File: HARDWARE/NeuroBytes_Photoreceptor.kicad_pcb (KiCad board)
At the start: 2 copper layers, 46.8 x 19.8 mm, 24 parts, among them P1 JST_GH_4-POS, P2 JST_GH_4-POS, P3 JST_GH_5-pos, SW1 SW_PB_4term, SW2 SW_PB_4term, U1 APDS9007, U2 STM32L011Gx, U3 3v3 LDO

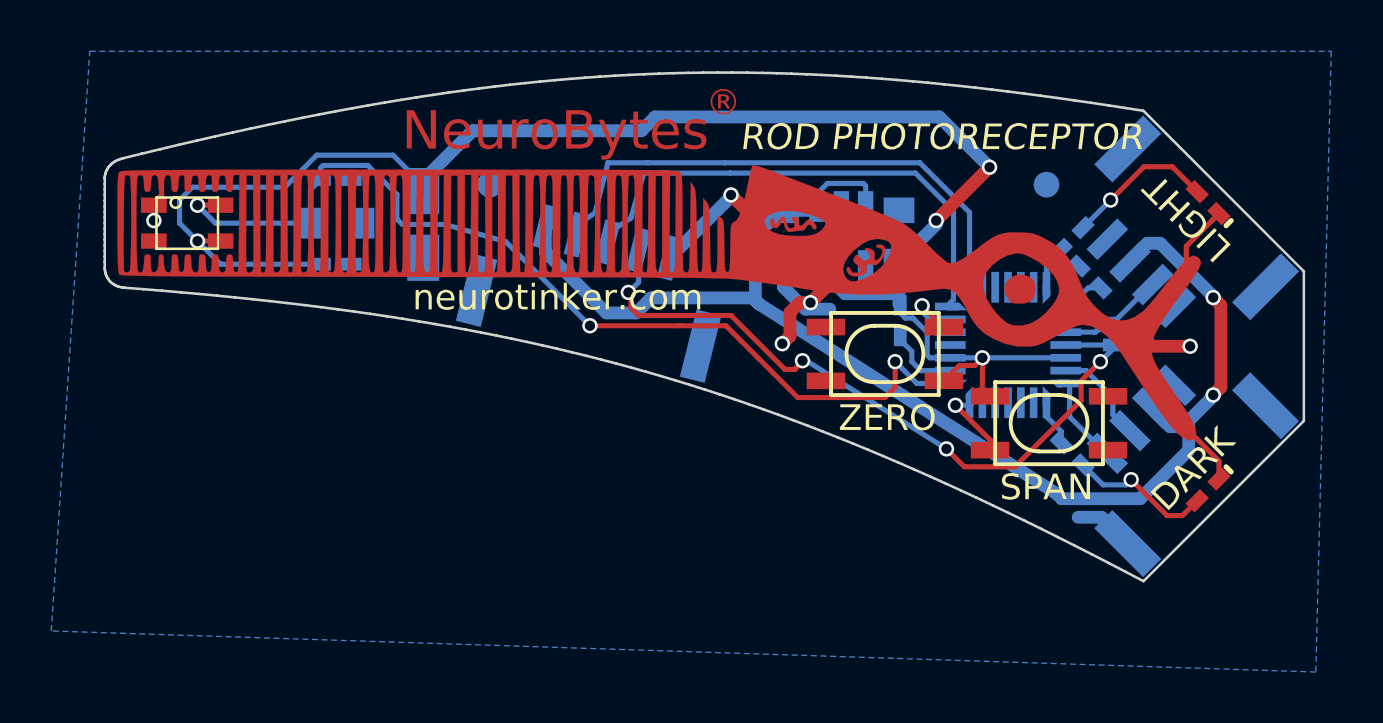
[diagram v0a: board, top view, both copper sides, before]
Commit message: added ESD protection. updated title block. minor routing changes.
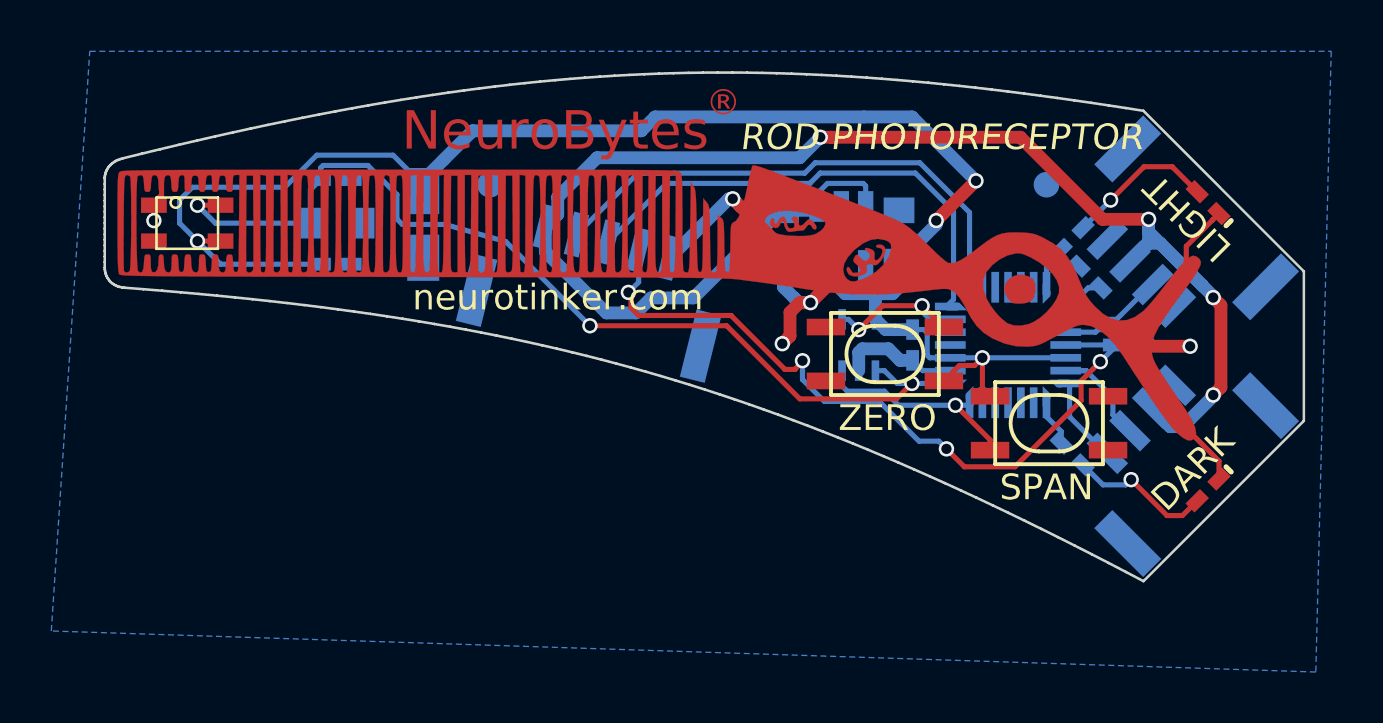
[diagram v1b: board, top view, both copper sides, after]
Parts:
- added U4: RClamp0503F, KiCad_Footprints:ZF_SMD_SOT-353, B.Cu at (194.2, 100.8)
- moved C6 1.06 mm to (196.3, 100.8)
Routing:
- net +5V: track 52.3 -> 61.7 mm, vias 2 -> 4
- net SPAN: track 3.15 -> 8.48 mm
- net ZERO: track 2.77 -> 6.44 mm, vias 1 -> 2
- net RESET: track 28.1 -> 29.7 mm
- net GND: track 54.8 -> 53.3 mm
- net SENSE: track 38.6 -> 39.3 mm
- net +3V3: track 66.0 -> 65.4 mm
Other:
- board text removed: "POWER"

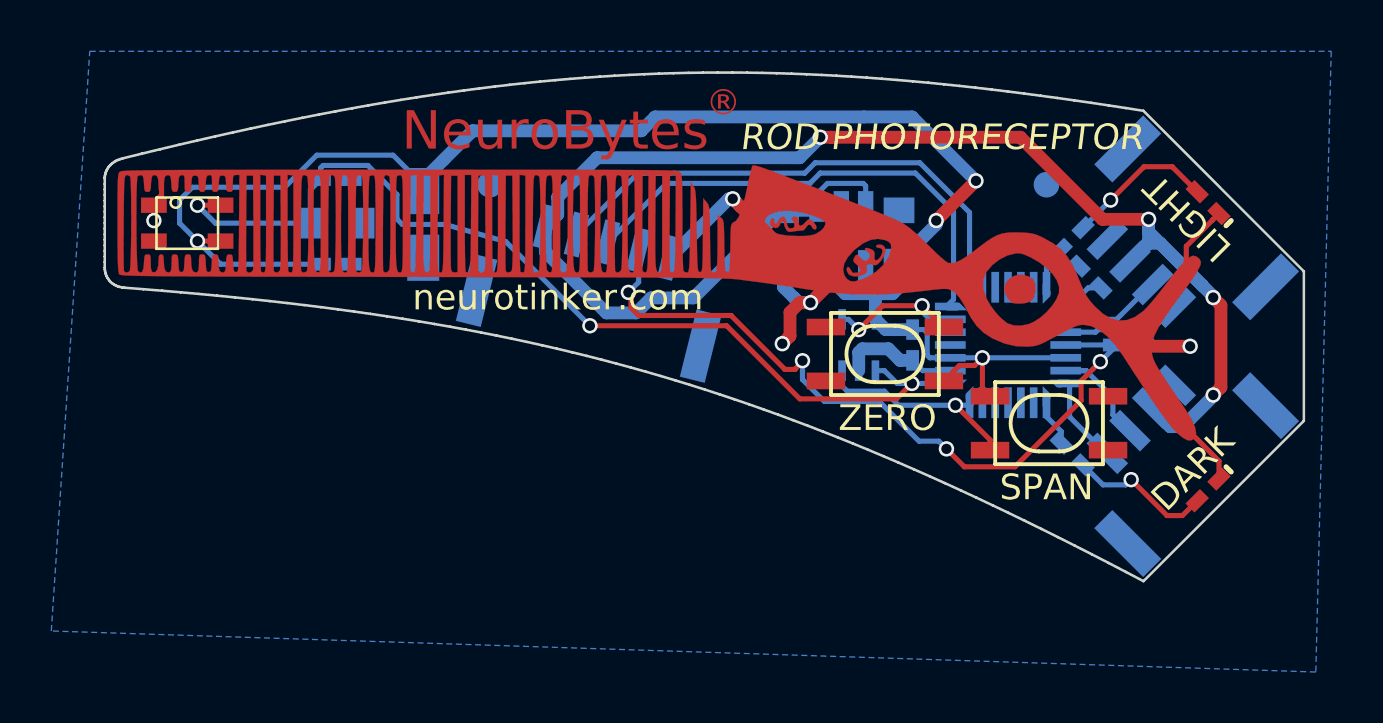
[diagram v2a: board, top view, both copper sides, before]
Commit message: updated footprints to include B.Fab outlines. minor routing changes. re-generated Gerbers. added placement pdf.
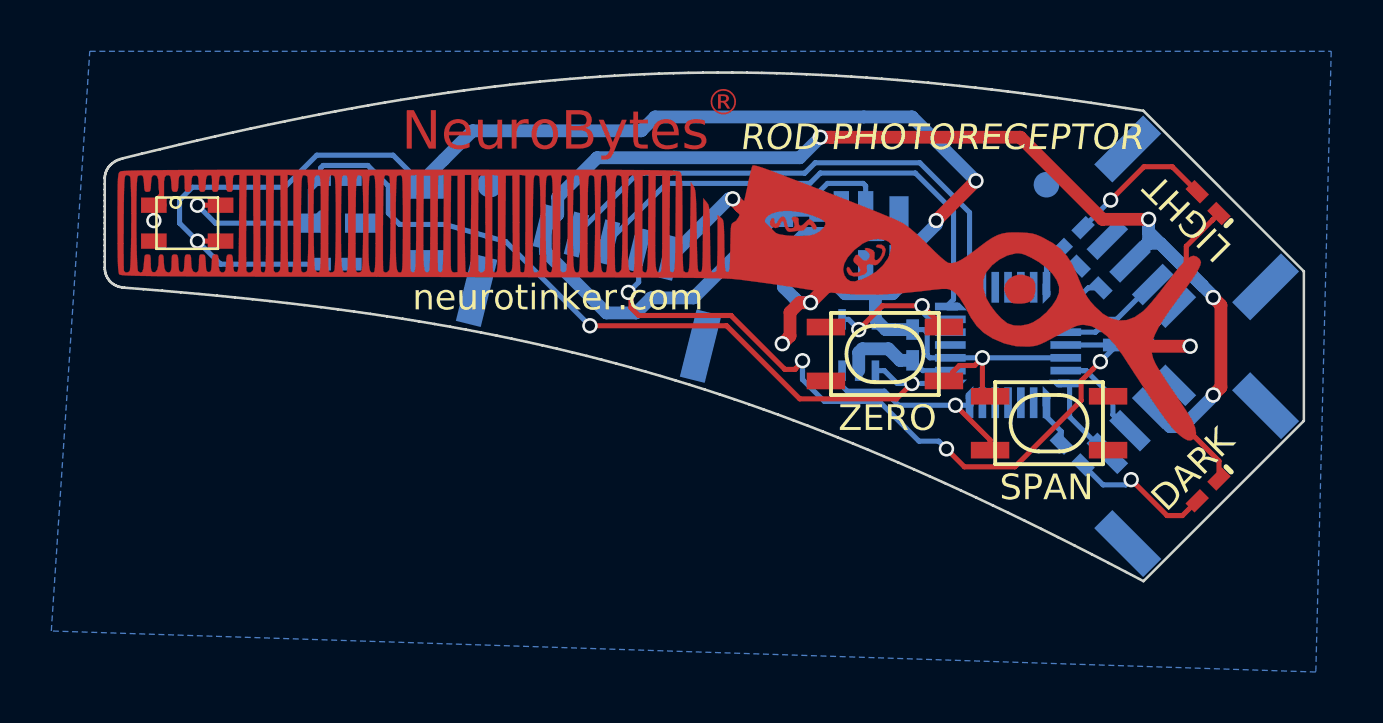
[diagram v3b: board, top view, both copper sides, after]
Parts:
- C3, C4, C5: footprint KiCad_Footprints:ZF_SMD_NonPol_0603 -> Capacitors_SMD:C_0603_HandSoldering
- C7: footprint KiCad_Footprints:ZF_SMD_nonpol_1206 -> Capacitors_SMD:C_1206
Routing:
- net GND: track 53.3 -> 59.8 mm
